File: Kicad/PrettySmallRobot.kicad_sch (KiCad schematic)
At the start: 56 parts, among them J1 TYPE-C-31-M-12, J2 MOTORA_1, J3 MOTORA_2, J4 MOTORB_1, J5 MOTORB_2, J6 BATT+, J7 GND, SW1 SW_Push, SW2 SW_Push, U1 DRV8837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

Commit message: ripped up all routing to start again to fit the new cad
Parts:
- removed U3: MCP73831-2ACI_MC, kicad_footprints:SON50P200X300X100-9N, symbol FSB-rescue:MCP73831-2ACI_MC-Kicad_symbols
- added J10, J9: Conn_01x02, Connector_JST:JST_PH_S2B-PH-K_1x02_P2.00mm_Horizontal, symbol Connector_Generic:Conn_01x02
- added J8: (no value), symbol Connector_Generic:Conn_01x02
- added U3: MCP73831-2-OT, Package_TO_SOT_SMD:SOT-23-5, symbol Battery_Management:MCP73831-2-OT
- BOOT1: renamed from SW1; LCSC TSA363G25-250B -> C231329
- H1: value (none) -> MountingHole; footprint (none) -> MountingHole:MountingHole_2.2mm_M2_DIN965_Pad
- H2: footprint (none) -> MountingHole:MountingHole_2.2mm_M2_DIN965_Pad
- Y1: LCSC (none) -> C252255
- renumbered SW2 to RST1
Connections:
- net +BATT: now also U3.3 (VBAT)
- net GND: now also U3.2 (VSS)
- net VBUS: now also U3.4 (VDD)
- net at R5.2: now also U3.1 (STAT)
- net at R6.2: now also U3.5 (PROG)

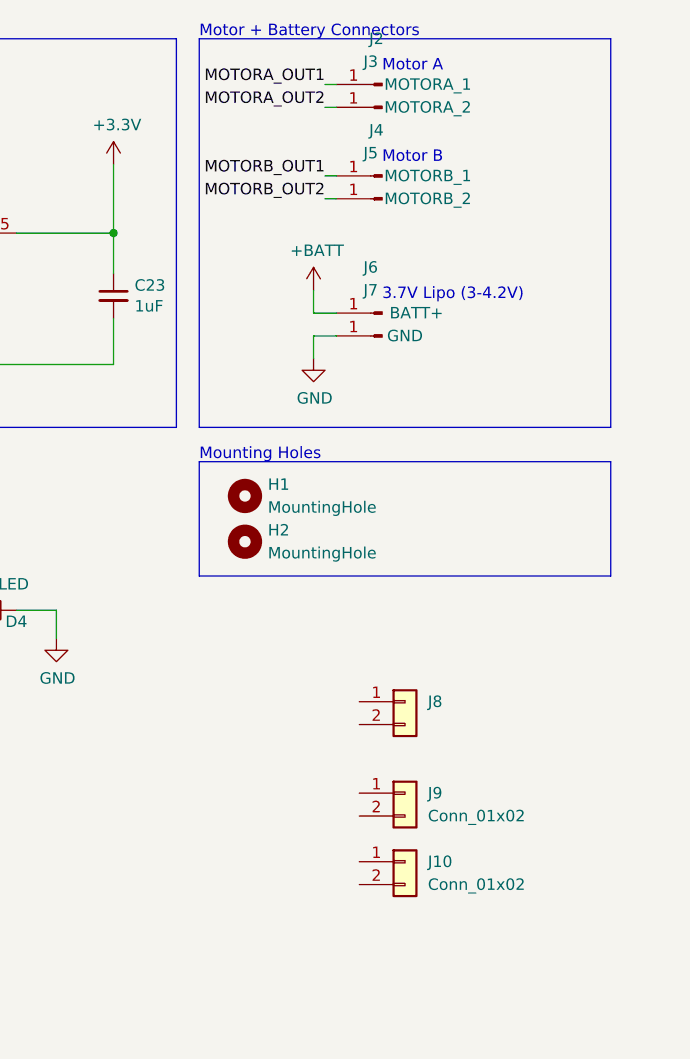
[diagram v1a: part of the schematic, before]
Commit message: re added jst connectors, removed mount holes
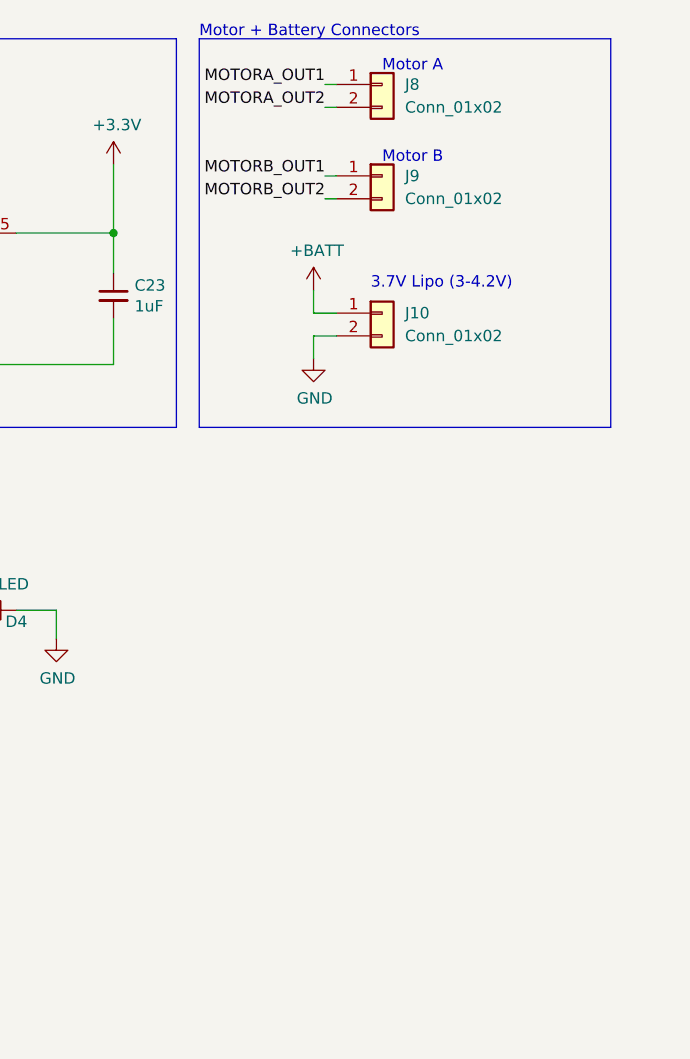
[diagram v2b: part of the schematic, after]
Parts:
- removed H1, H2: MountingHole, MountingHole:MountingHole_2.2mm_M2_DIN965_Pad, symbol Mechanical:MountingHole
- removed J2: MOTORA_1, Connector_Wire:SolderWirePad_1x01_SMD_1x2mm, symbol Connector:Conn_01x01_Male
- removed J3: MOTORA_2, Connector_Wire:SolderWirePad_1x01_SMD_1x2mm, symbol Connector:Conn_01x01_Male
- removed J4: MOTORB_1, Connector_Wire:SolderWirePad_1x01_SMD_1x2mm, symbol Connector:Conn_01x01_Male
- removed J5: MOTORB_2, Connector_Wire:SolderWirePad_1x01_SMD_1x2mm, symbol Connector:Conn_01x01_Male
- removed J6: BATT+, Connector_Wire:SolderWirePad_1x01_SMD_1x2mm, symbol Connector:Conn_01x01_Male
- removed J7: GND, Connector_Wire:SolderWirePad_1x01_SMD_1x2mm, symbol Connector:Conn_01x01_Male
- J8: value (none) -> Conn_01x02; footprint (none) -> Connector_JST:JST_PH_S2B-PH-K_1x02_P2.00mm_Horizontal
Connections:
- net +BATT: now also J10.1 (Pin_1)
- net GND: now also J10.2 (Pin_2)
- net MOTORA_OUT1: now also J8.1 (Pin_1)
- net MOTORA_OUT2: now also J8.2 (Pin_2)
- net MOTORB_OUT1: now also J9.1 (Pin_1)
- net MOTORB_OUT2: now also J9.2 (Pin_2)
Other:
- note removed: "Mounting Holes"
- moved on the sheet: J10, J8, J9

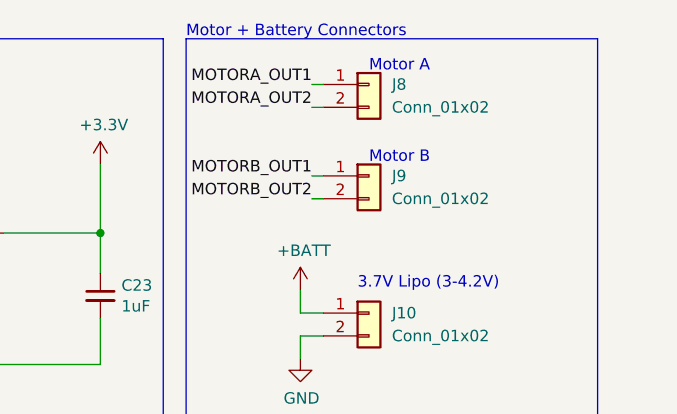
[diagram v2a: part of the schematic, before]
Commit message: swapped motor a and b connectors
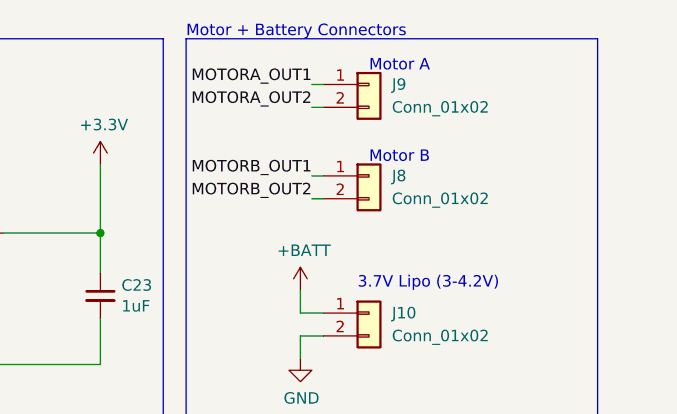
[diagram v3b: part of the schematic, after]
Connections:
- net MOTORA_OUT1: now also J9.1 (Pin_1); no longer J8.1 (Pin_1)
- net MOTORA_OUT2: now also J9.2 (Pin_2); no longer J8.2 (Pin_2)
- net MOTORB_OUT1: now also J8.1 (Pin_1); no longer J9.1 (Pin_1)
- net MOTORB_OUT2: now also J8.2 (Pin_2); no longer J9.2 (Pin_2)
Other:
- moved on the sheet: J8, J9

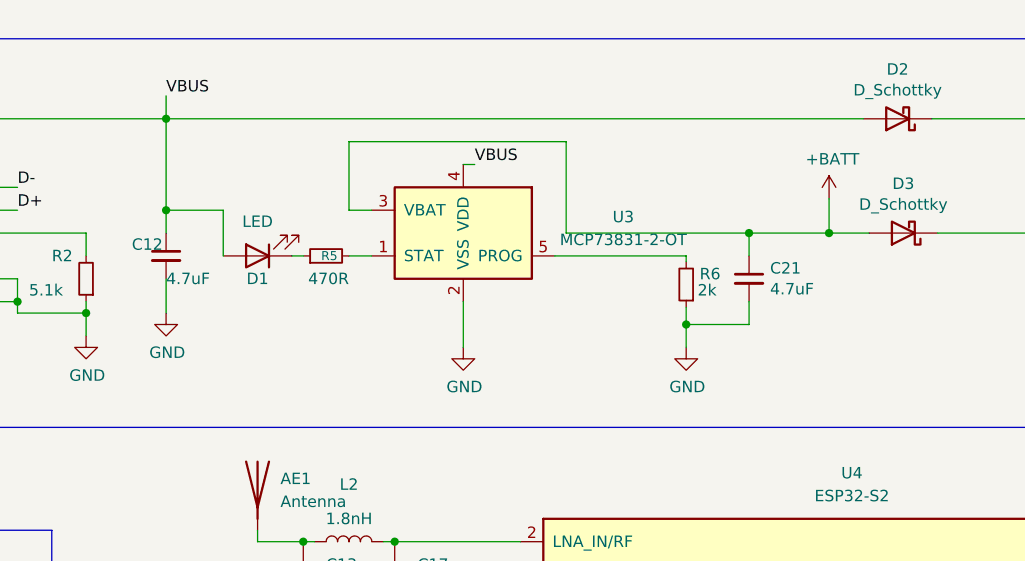
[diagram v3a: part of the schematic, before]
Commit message: changed mcp 73831 to diff package in stock on jlcpcb
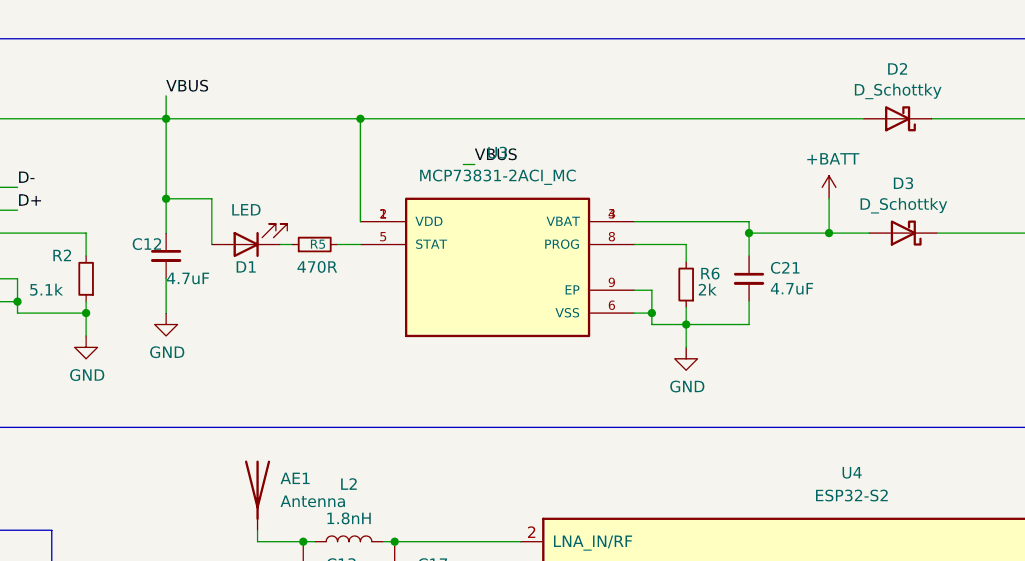
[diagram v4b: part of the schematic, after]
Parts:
- removed U3: MCP73831-2-OT, Package_TO_SOT_SMD:SOT-23-5, symbol Battery_Management:MCP73831-2-OT
- added U3: MCP73831-2ACI_MC, symbol Kicad_symbols:MCP73831-2ACI_MC
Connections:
- net +BATT: now also U3.3 (VBAT), U3.4 (VBAT)
- net GND: now also U3.6 (VSS), U3.9 (EP)
- net VBUS: now also U3.1 (VDD), U3.2 (VDD)
- net at R5.2: now also U3.5 (STAT)
- net at R6.2: now also U3.8 (PROG)
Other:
- moved on the sheet: D1, R5

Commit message: update to latest
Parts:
- U3: footprint (none) -> kicad_footprints:SON50P200X300X100-9N; LCSC (none) -> C150772
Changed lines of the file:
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@@
     (property "Reference" "U3" (id 0) (at 123.19 29.21 0))
     (property "Value" "MCP73831-2ACI_MC" (id 1) (at 123.19 31.75 0))
-    (property "Footprint" "" (id 2) (at 123.19 41.91 0)
+    (property "Footprint" "kicad_footprints:SON50P200X300X100-9N" (id 2) (at 123.19 41.91 0)
       (effects (font (size 1.27 1.27)) (justify left bottom) hide)
     )
@@
       (effects (font (size 1.27 1.27)) (justify left bottom) hide)
     )
+    (property "LCSC" "C150772" (id 7) (at 123.19 41.91 0)
+      (effects (font (size 1.27 1.27)) hide)
+    )
     (pin "1")

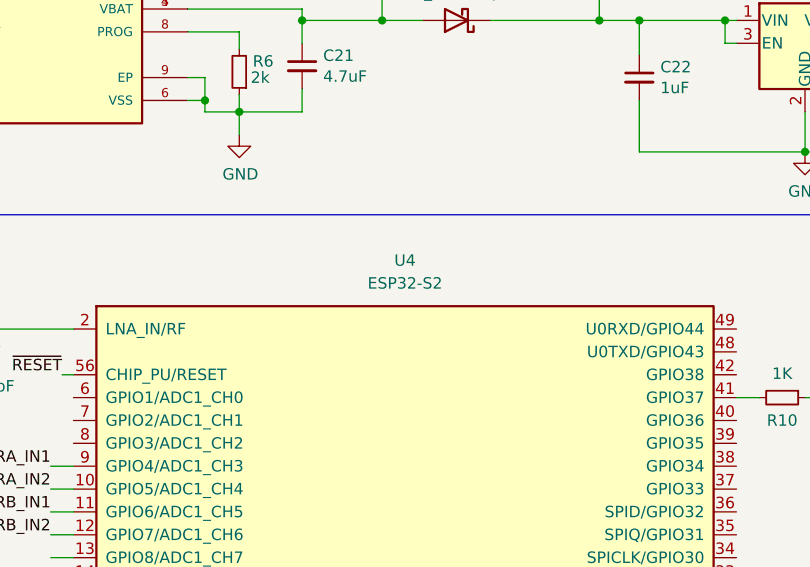
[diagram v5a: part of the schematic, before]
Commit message: added mqtt remote control stuff
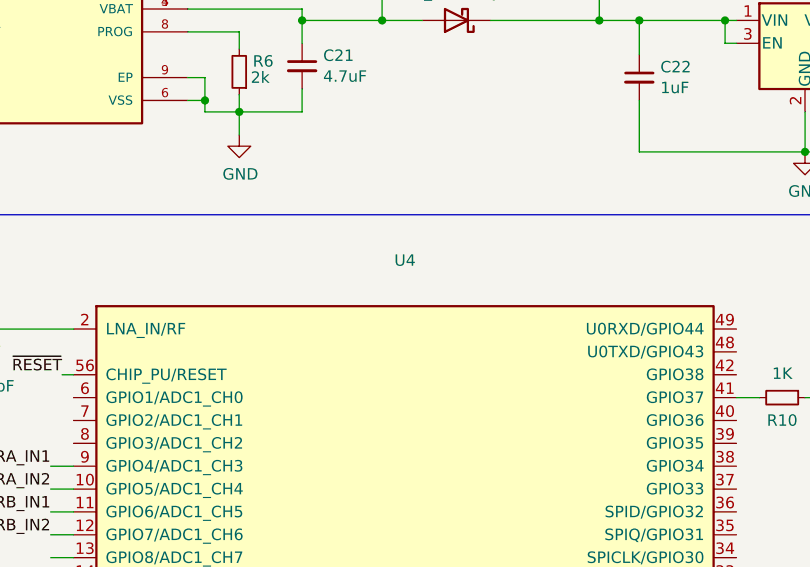
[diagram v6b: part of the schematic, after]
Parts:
- U4: value ESP32-S2 -> (none); footprint Package_DFN_QFN:QFN-56-1EP_7x7mm_P0.4mm_EP5.6x5.6mm -> (none)
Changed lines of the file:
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@@
     (in_bom yes) (on_board yes) (fields_autoplaced)
     (property "Reference" "U4" (id 0) (at 162.56 64.77 0))
-    (property "Value" "ESP32-S2" (id 1) (at 162.56 67.31 0))
-    (property "Footprint" "Package_DFN_QFN:QFN-56-1EP_7x7mm_P0.4mm_EP5.6x5.6mm" (id 2) (at 161.29 161.29 0)
+    (property "Value" "" (id 1) (at 162.56 67.31 0))
+    (property "Footprint" "" (id 2) (at 161.29 161.29 0)
       (effects (font (size 1.27 1.27)) hide)
     )
@@
     )
     (path "/8bff7f3c-8391-47bd-8438-7e4af69ca5f3"
-      (reference "U4") (unit 1) (value "ESP32-S2") (footprint "Package_DFN_QFN:QFN-56-1EP_7x7mm_P0.4mm_EP5.6x5.6mm")
+      (reference "U4") (unit 1) (value "ESP32-S2FN4R2") (footprint "Package_DFN_QFN:QFN-56-1EP_7x7mm_P0.4mm_EP5.6x5.6mm")
     )
     (path "/1f286913-efd4-4446-a7df-9b5ef97d915e"
